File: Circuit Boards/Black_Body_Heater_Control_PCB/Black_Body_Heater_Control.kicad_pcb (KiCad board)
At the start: 2 copper layers, 57.5 x 42.8 mm, 57 parts, among them J201 5040500891, J202 Conn_01x04_Pin, J203 USB_C_Receptacle_USB2.0_16P, P301 436500200, P302 436500200, Q302 BD139, SW201 SW_MEC_5E, SW202 SW_MEC_5E, U201 AMS1117-3.3, U202 ESP32-S3-WROOM-1-N8R8, U203 USBLC6-2SC6, U301 DAC60501ZDGSR, U302 INA181A2IDBVR, U304 LMR51420XFDDCR, U305 LM358

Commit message: Required Schematic changes made
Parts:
- removed C305, C306: 100nf, Capacitor_SMD:C_0603_1608Metric
- removed C307, C308, C309: 10uf, Capacitor_SMD:C_0603_1608Metric
- removed L301: SRR1208-120ML, -inductors:SRR1208
- removed U304: LMR51420XFDDCR, Package_TO_SOT_SMD:SOT-23-6
- added J301: Conn_01x02_Pin, Connector_PinHeader_1.27mm:PinHeader_1x02_P1.27mm_Vertical, F.Cu at (126.3, 135.2)
- added U303: ~, -buck:TPSM84209, F.Cu at (121.2, 136.8)
- C302: value 1uf -> 6.8uf
- C303: value 1uf -> 330pf
- C304: value 1uf -> 47uf; footprint Capacitor_SMD:C_0603_1608Metric -> Capacitor_SMD:C_1210_3225Metric
- R309: value 162k -> 10k
- R310: value 22.6k -> 1.37k
- moved R309 23.0 mm to (120.5, 131.0)
- moved R310 23.0 mm to (123.5, 131.0)
- moved C302 17.3 mm to (136.5, 135.0)
- moved C304 16.9 mm to (133.9, 135.0)
- moved C303 15.8 mm to (131.0, 134.2)
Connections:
- C303 pad 1: VCC -> +5V
- C303 pad 2: GND -> Net-(U303-FB)
- C304 pad 1: VCC -> +5V
- R309 pad 1: /Power_periferals/FB -> +5V
- R309 pad 2: +5V -> Net-(U303-FB)
- R310 pad 1: GND -> Net-(U303-FB)
- R310 pad 2: /Power_periferals/FB -> GND
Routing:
- net (no net): track 0.00 -> 9.65 mm
- net /Power_periferals/FB: track 7.95 -> 0.00 mm
- net /Power_periferals/CB: track 1.70 -> 0.00 mm
- net Net-(U303-FB): track 0.00 -> 1.08 mm, vias 0 -> 1
- net GND: track 29.4 -> 28.3 mm, vias 78 -> 77
- added copper zone on F.Cu, net (none)
- removed copper zone on F.Cu, net /Power_periferals/CB
- removed copper zone on F.Cu, net /Power_periferals/SW

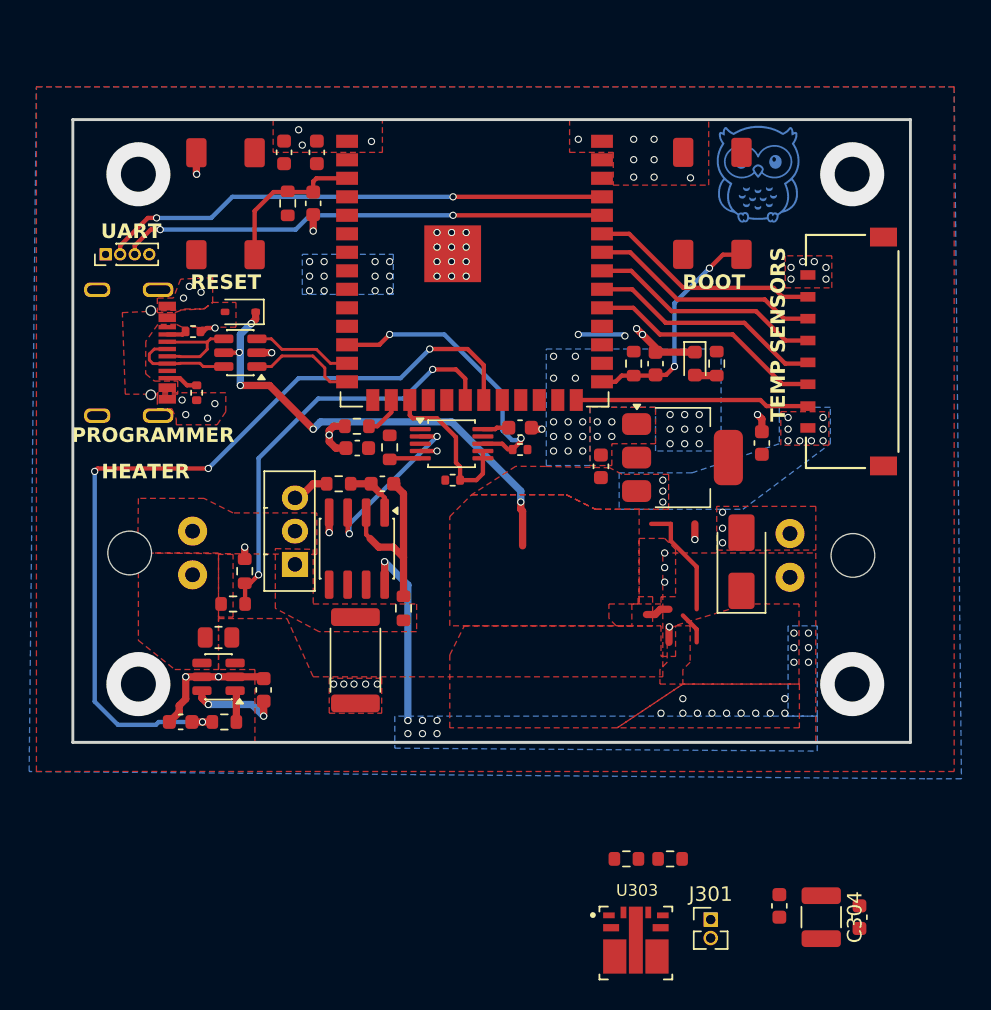
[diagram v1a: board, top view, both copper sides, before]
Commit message: Changing buck on heater pcb
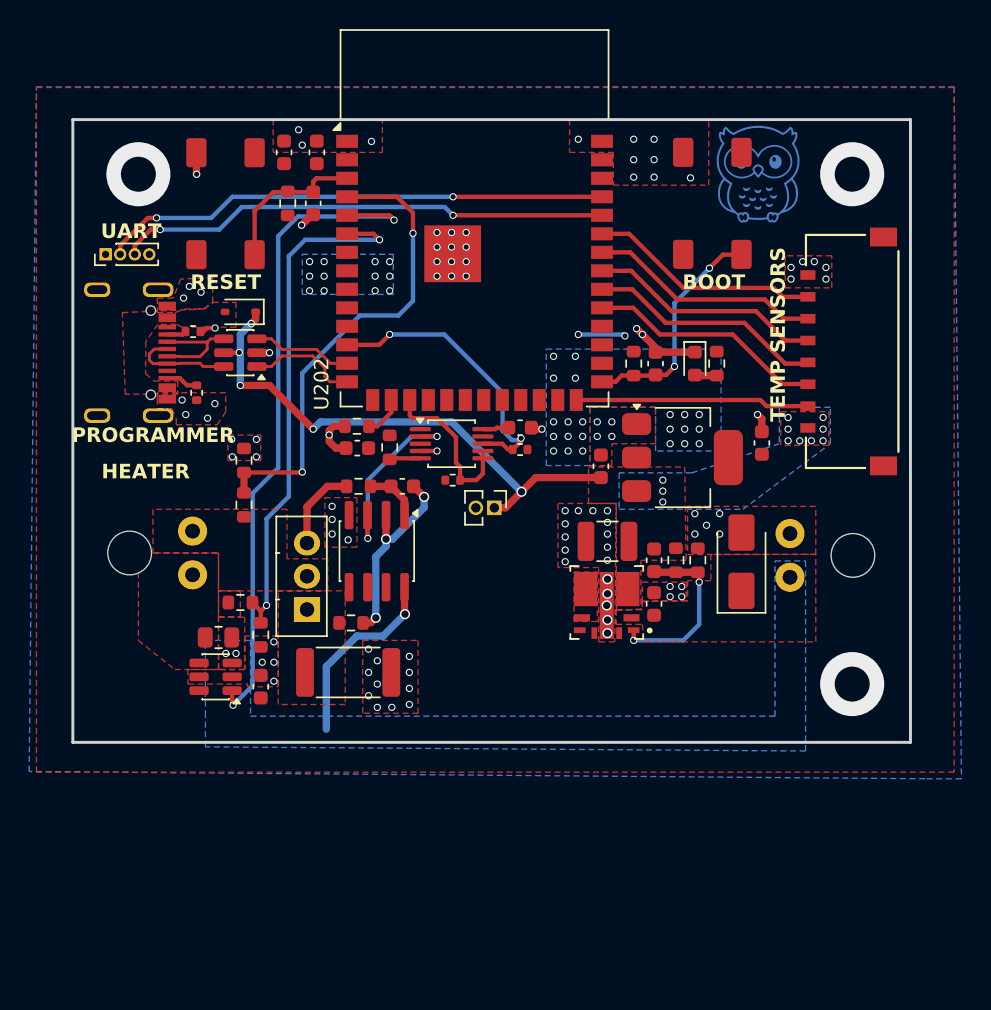
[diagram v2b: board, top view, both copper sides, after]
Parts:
- removed C205: 1uf, Capacitor_SMD:C_0603_1608Metric
- removed R204: 10k, Resistor_SMD:R_0603_1608Metric
- added R312: 100k, Resistor_SMD:R_0603_1608Metric, F.Cu at (94.2, 106.7)
- added R313: 10k, Resistor_SMD:R_0603_1608Metric, F.Cu at (94.2, 103.7)
- U202: footprint -mcu:ESP32-S3-WROOM-1 -> RF_Module:ESP32-S3-WROOM-1
- moved J301 31.9 mm to (111.4, 106.9), turned to -90 degrees
- moved C304 29.7 mm to (119.2, 109.2), turned to 180 degrees
- moved C302 25.7 mm to (122.4, 113.5), turned to 90 degrees
- moved C303 25.2 mm to (122.4, 110.5)
- moved U303 23.5 mm to (119.2, 113.4), turned to 180 degrees
- moved R309 20.8 mm to (123.9, 110.5), turned to -90 degrees
- moved R310 20.6 mm to (125.4, 110.5), turned to 90 degrees
- moved R308 4.51 mm to (95.4, 115.6), turned to 90 degrees
- moved R304 3.74 mm to (101.6, 114.8), turned to 180 degrees
- moved Q302 3.21 mm to (98.6, 113.9)
- moved C301 1.38 mm to (105.1, 105.4)
- moved R305 1.38 mm to (102.1, 105.4)
- moved U305 1.38 mm to (103.4, 109.9)
- moved R306 0.98 mm to (101.4, 118.2), turned to 0 degrees
- moved R307 0.51 mm to (94.0, 113.4)
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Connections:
- R307 pad 1: /ESP32/V_SENSE -> /ESP32/V_SENSE+
- R308 pad 2: /ESP32/V_SENSE -> /ESP32/V_SENSE+
- U202 pad 20: /ESP32/V_SENSE -> unconnected-(U202-IO12-Pad20)
- U202 pad 21: /ESP32/IO13 -> unconnected-(U202-IO13-Pad21)
- U202 pad 4: unconnected-(U202-IO4-Pad4) -> /ESP32/V_SENSE-
- U202 pad 5: unconnected-(U202-IO5-Pad5) -> /ESP32/I_SENSE
- U202 pad 6: unconnected-(U202-IO6-Pad6) -> /ESP32/V_SENSE+
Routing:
- net /ESP32/IO13: track 58.6 -> 0.00 mm, vias 4 -> 0
- net /ESP32/I_SENSE: track 2.19 -> 46.5 mm, vias 0 -> 2
- net /ESP32/V_SENSE+: track 0.00 -> 36.1 mm, vias 0 -> 2
- net /ESP32/V_SENSE-: track 0.00 -> 32.9 mm, vias 0 -> 2
- net /ESP32/V_SENSE: track 29.1 -> 0.00 mm, vias 2 -> 0
- net GND: track 28.3 -> 15.9 mm, vias 77 -> 99
- net Net-(U303-FB): track 1.08 -> 12.3 mm, vias 1 -> 2
- net (no net): track 9.65 -> 0.00 mm, vias 4 -> 3
- net +3V3: track 9.53 -> 3.24 mm, vias 38 -> 36
- net +5V: track 33.0 -> 37.5 mm
- net /Power_periferals/fet_in: track 2.58 -> 5.79 mm
- net VCC: track 15.4 -> 13.1 mm, vias 13 -> 3
- net /Power_periferals/vout: track 11.9 -> 12.8 mm
- net /Power_periferals/neg_fdbk: track 13.0 -> 13.1 mm, vias 0 -> 3
- added copper zone on F.Cu, net Net-(U303-SW-Pad4)
- removed copper zone on F.Cu, net (none)

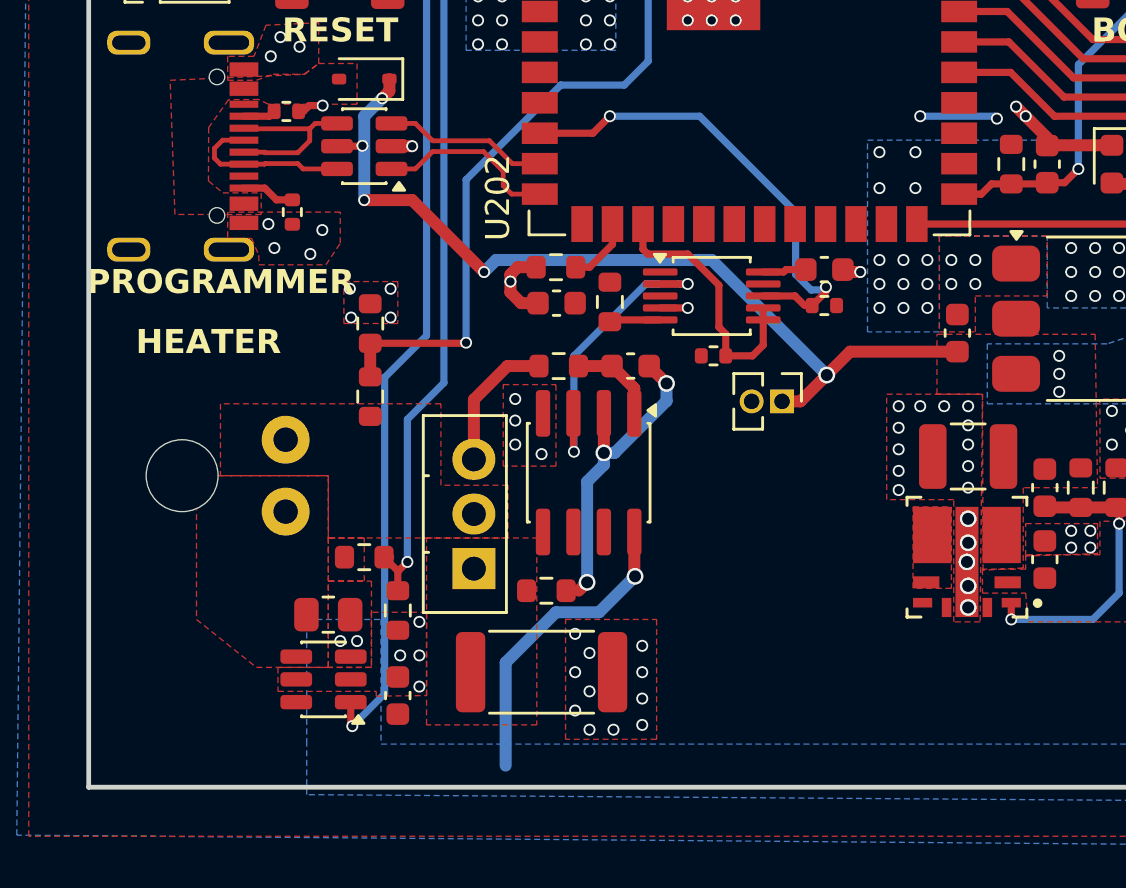
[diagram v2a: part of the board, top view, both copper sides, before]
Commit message: Heater control rev 1 ordered
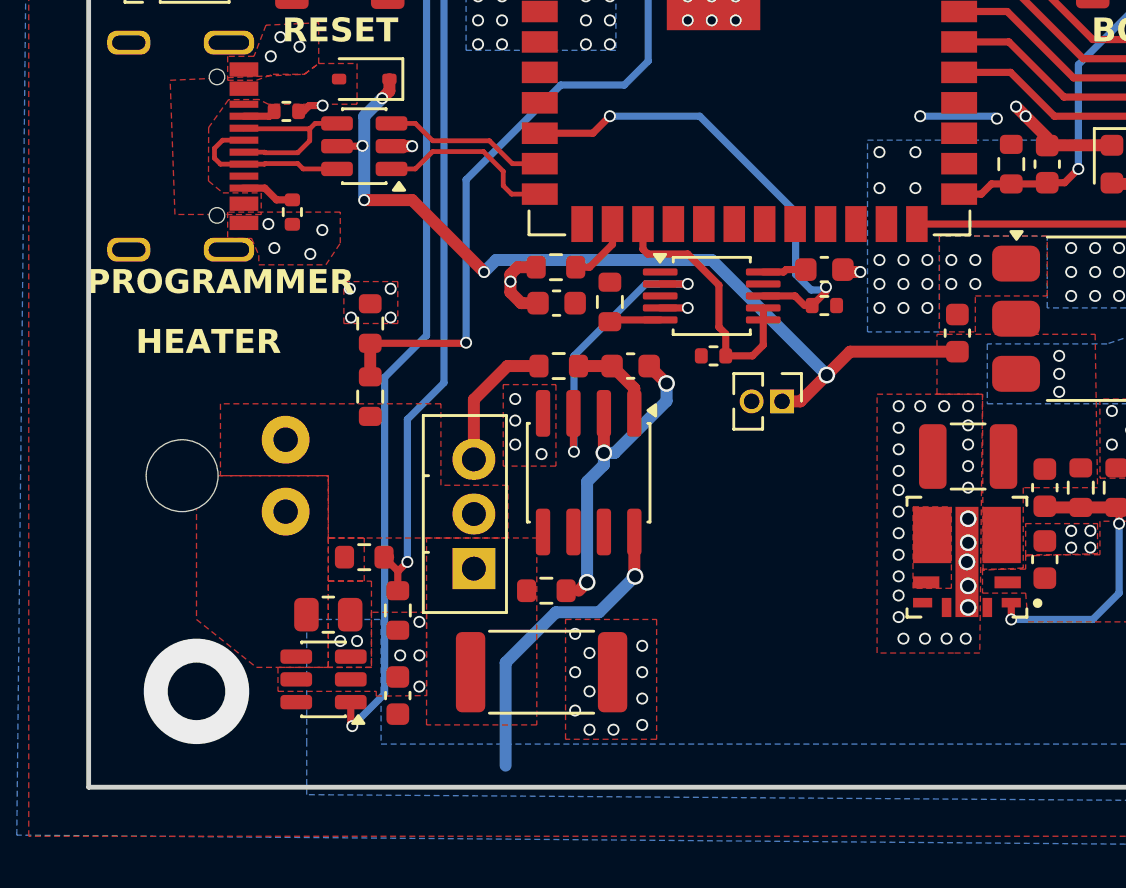
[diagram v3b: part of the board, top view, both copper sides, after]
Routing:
- net GND: vias 99 -> 109
- net (no net): vias 3 -> 4
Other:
- board text added: "Black Body Heater Controler REV. 1"
- board text removed: "Black Body Heater Controler REV. 0"
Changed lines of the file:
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@@
 		(capping no)
 		(filling no)
+		(zone_defaults)
 		(pcbplotparams
 			(layerselection 0x00000000_00000000_55555555_5755f5ff)
@@
 			(unlocked yes)
 			(layer "F.SilkS")
+			(hide yes)
 			(effects
 				(font
@@
 		(sheetname "/ESP32/")
 		(sheetfile "ESP32.kicad_sch")
+		(units
+			(unit
+				(name "A")
+				(pins "3" "27" "39" "38" "15" "4" "5" "6" "7" "12" "17" "18" "19" "20"
+					"21" "22" "8" "9" "2" "41" "40" "1" "37" "36" "10" "11" "13" "14" "23"
+					"28" "29" "30" "31" "32" "33" "34" "35" "26" "16" "24" "25"
+				)
+			)
+		)
 		(attr smd)
 		(duplicate_pad_numbers_are_jumpers no)
@@
 			)
 		)
-		(property "MPN" "CRCW0603162KFKEA"
+		(property "MPN" "ERA-3AEB103V"
 			(at 0 0 270)
 			(unlocked yes)
@@
 			)
 		)
+		(property "MPN" "TPSM84209RKHR"
+			(at 0 0 180)
+			(unlocked yes)
+			(layer "F.Fab")
+			(hide yes)
+			(effects
+				(font
+					(size 1 1)
+					(thickness 0.15)
+				)
+			)
+		)
 		(sheetname "/Power_periferals/")
 		(sheetfile "power_periferals.kicad_sch")
@@
 			)
 		)
-		(property "MPN" "C0603C105K4RACTU"
+		(property "MPN" "C0603C331J5GACTU"
 			(at 0 0 270)
 			(unlocked yes)
@@
 			)
 		)
-		(attr through_hole)
+		(attr through_hole exclude_from_bom dnp)
 		(duplicate_pad_numbers_are_jumpers no)
 		(fp_line
@@
 			)
 		)
-		(property "MPN" "ERA-3AEB2262V"
+		(property "MPN" "ERJ-3EKF1371V"
 			(at 0 0 90)
 			(unlocked yes)
@@
 			)
 		)
-		(property "MPN" "C0603C105K4RACTU"
+		(property "MPN" "C1608X5R1E685K080AC"
 			(at 0 0 90)
 			(unlocked yes)
@@
 			)
 		)
+		(property "MPN" "GRM32EC81C476KE15L"
+			(at 0 0 180)
+			(unlocked yes)
+			(layer "F.Fab")
+			(hide yes)
+			(effects
+				(font
+					(size 1 1)
+					(thickness 0.15)
+				)
+			)
+		)
 		(property ki_fp_filters "C_*")
 		(sheetname "/Power_periferals/")
@@
 		)
 	)
-	(gr_text "Black Body Heater Controler REV. 0"
-		(at 132.5 120 0)
+	(gr_text "-\n\n+"
+		(at 113.1 106.9 90)
+		(layer "B.SilkS")
+		(effects
+			(font
+				(size 1 1)
+				(thickness 0.2)
+				(bold yes)
+			)
+			(justify bottom mirror)
+		)
+	)
+	(gr_text "Black Body Heater Controler REV. 1"
+		(at 132.6 120.929362 0)
 		(layer "B.SilkS")
 		(effects
@@
 	)
 	(gr_text_box "Programming Mode:\n1. Hold BOOT\n2. Press RESET\n3. Release RESET\n3. Release BOOT"
-		(start 105.2 107.229362)
-		(end 122.2 117.370638)
+		(start 105.3 108.158724)
+		(end 122.3 118.3)
 		(margins 1.0025 1.0025 1.0025 1.0025)
 		(layer "B.SilkS")
@@
 	)
 	(via
+		(at 87 119)
+		(size 4.4)
+		(drill 2.4)
+		(layers "F.Cu" "B.Cu")
+		(free yes)
+		(tenting
+			(front no)
+			(back no)
+		)
+		(capping no)
+		(covering
+			(front no)
+			(back no)
+		)
+		(plugging
+			(front no)
+			(back no)
+		)
+		(filling no)
+		(net "")
+	)
+	(via
 		(at 136 84)
 		(size 4.4)
@@
 	)
 	(via
+		(at 116.3 113.3)
+		(size 0.5)
+		(drill 0.35)
+		(layers "F.Cu" "B.Cu")
+		(free yes)
+		(net "GND")
+	)
+	(via
 		(at 93.4 102.2)
 		(size 0.5)
@@
 	)
 	(via
+		(at 116.3 111.5)
+		(size 0.5)
+		(drill 0.35)
+		(layers "F.Cu" "B.Cu")
+		(free yes)
+		(net "GND")
+	)
+	(via
 		(at 102.8 116.6)
 		(size 0.5)
@@
 	)
 	(via
+		(at 119.1 116.8)
+		(size 0.5)
+		(drill 0.35)
+		(layers "F.Cu" "B.Cu")
+		(free yes)
+		(net "GND")
+	)
+	(via
+		(at 118.3 116.8)
+		(size 0.5)
+		(drill 0.35)
+		(layers "F.Cu" "B.Cu")
+		(free yes)
+		(net "GND")
+	)
+	(via
 		(at 91 84)
 		(size 0.5)
@@
 	)
 	(via
+		(at 117.4 116.8)
+		(size 0.5)
+		(drill 0.35)
+		(layers "F.Cu" "B.Cu")
+		(free yes)
+		(net "GND")
+	)
+	(via
 		(at 118.2 107.1)
 		(size 0.5)
@@
 	)
 	(via
+		(at 116.3 114.2)
+		(size 0.5)
+		(drill 0.35)
+		(layers "F.Cu" "B.Cu")
+		(free yes)
+		(net "GND")
+	)
+	(via
 		(at 108.5 91)
 		(size 0.5)
@@
 	)
 	(via
+		(at 116.5 116.8)
+		(size 0.5)
+		(drill 0.35)
+		(layers "F.Cu" "B.Cu")
+		(free yes)
+		(net "GND")
+	)
+	(via
 		(at 103 81.75)
 		(size 0.5)
@@
 	)
 	(via
+		(at 116.3 115)
+		(size 0.5)
+		(drill 0.35)
+		(layers "F.Cu" "B.Cu")
+		(free yes)
+		(net "GND")
+	)
+	(via
 		(at 108.5 90)
 		(size 0.5)
@@
 	)
 	(via
+		(at 116.3 115.9)
+		(size 0.5)
+		(drill 0.35)
+		(layers "F.Cu" "B.Cu")
+		(free yes)
+		(net "GND")
+	)
+	(via
 		(at 119.5 102)
 		(size 0.5)
@@
 	)
 	(via
+		(at 116.3 112.4)
+		(size 0.5)
+		(drill 0.35)
+		(layers "F.Cu" "B.Cu")
+		(free yes)
+		(net "GND")
+	)
+	(via
 		(at 92.263532 94.555748)
 		(size 0.5)
@@
 		(polygon
 			(pts
-				(xy 119.7 116.1) (xy 118.6 116.1) (xy 118.6 111) (xy 115.8 111) (xy 115.8 106.6) (xy 119.8 106.6)
+				(xy 119.686316 117.4) (xy 118.6 117.4) (xy 115.4 117.4) (xy 115.4 106.6) (xy 119.8 106.6)
 			)
 		)
@@
 		(layer "F.Cu")
 		(hatch edge 0.5)
-		(priority 11)
+		(priority 28)
 		(connect_pads thru_hole_only
 			(clearance 0.2)
